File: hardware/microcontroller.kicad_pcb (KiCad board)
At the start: 2 copper layers, 50.8 x 78.7 mm, 45 parts, among them J5 1x2 jumper right-angle, J6 Conn_02x03_Odd_Even, J7 1x2 jumper right-angle, U1 74LVC2G125, U10 74HC670, U11 74HC670, U13 74AHC74, U15 74LVC138A, U17 74LVC138A, U18 74LVC2G125, U3 74LV163, U4 74LV163, U5 74LV163, U6 74LV163, U7 74LV163, U8 74LV164, U9 74LV164

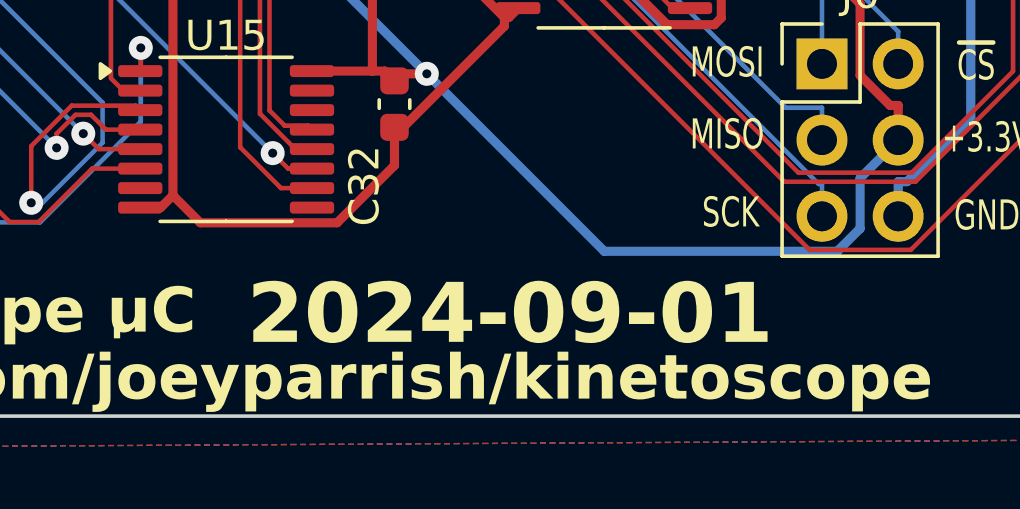
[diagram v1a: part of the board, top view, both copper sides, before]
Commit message: Improve uC board assembly process, fix minor bug
Changes to part numbers to better align with JLCPCB stock:
 - Replace 74LV164PW,118 / C179331 with SN74LV164APWR / C403720
 - Replace SN74LV163APWR / C2675453 with SN74LV161APWR / C2649404
   - Original had sync clear, but this is async clear, which is a bug
     fix!
 - Fix rotation of U8, U9, U13
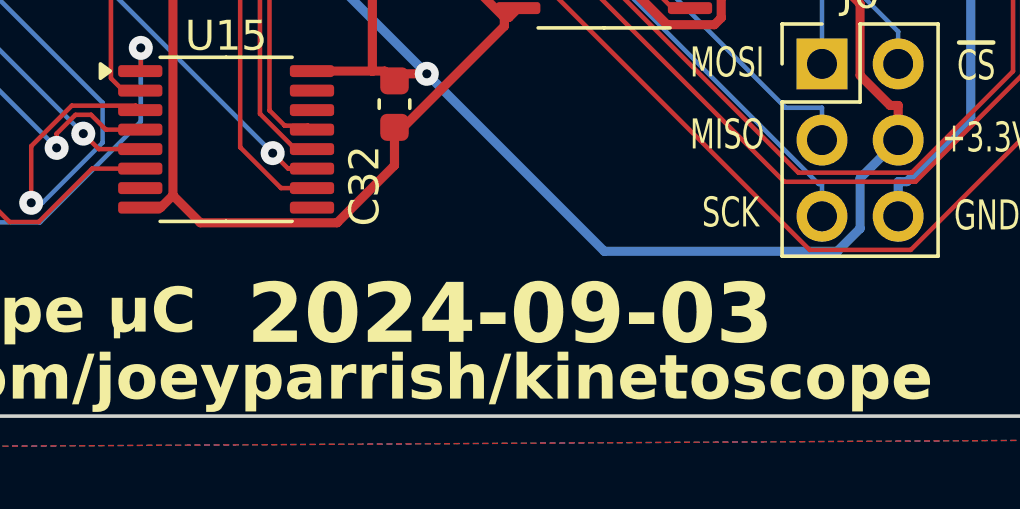
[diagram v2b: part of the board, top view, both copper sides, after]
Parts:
- U3, U4, U5, U6, U7: value 74LV163 -> 74LV161A
- U8, U9: value 74LV164 -> 74LV164A
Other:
- board text added: "2024-09-03"
- board text removed: "2024-09-01"
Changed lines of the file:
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@@
 			)
 		)
-		(property "Value" "74LV164"
+		(property "Value" "74LV164A"
 			(at 0 3.45 0)
 			(layer "F.Fab")
@@
 			)
 		)
-		(property "Datasheet" "https://www.mouser.com/datasheet/2/916/74LV164-1517637.pdf"
+		(property "Datasheet" "https://www.ti.com/lit/gpn/sn74lv164a"
 			(at 0 0 0)
 			(unlocked yes)
@@
 			)
 		)
-		(property "Mouser Part Number" "771-LV164PW118"
+		(property "Mouser Part Number" "595-SN74LV164APWR"
 			(at 0 0 0)
 			(unlocked yes)
@@
 			)
 		)
-		(property "Part Number" "74LV164PW,118"
+		(property "Part Number" "SN74LV164APWR"
 			(at 0 0 0)
 			(unlocked yes)
@@
 			)
 		)
-		(property "JLCPCB Part Number" "C179331"
+		(property "JLCPCB Part Number" "C403720"
 			(at 0 0 0)
 			(unlocked yes)
@@
 			)
 		)
-		(property "Value" "74LV164"
+		(property "Value" "74LV164A"
 			(at 0 3.45 0)
 			(layer "F.Fab")
@@
 			)
 		)
-		(property "Datasheet" "https://www.mouser.com/datasheet/2/916/74LV164-1517637.pdf"
+		(property "Datasheet" "https://www.ti.com/lit/gpn/sn74lv164a"
 			(at 0 0 0)
 			(unlocked yes)
@@
 			)
 		)
-		(property "Mouser Part Number" "771-LV164PW118"
+		(property "Mouser Part Number" "595-SN74LV164APWR"
 			(at 0 0 0)
 			(unlocked yes)
@@
 			)
 		)
-		(property "Part Number" "74LV164PW,118"
+		(property "Part Number" "SN74LV164APWR"
 			(at 0 0 0)
 			(unlocked yes)
@@
 			)
 		)
-		(property "JLCPCB Part Number" "C179331"
+		(property "JLCPCB Part Number" "C403720"
 			(at 0 0 0)
 			(unlocked yes)
@@
 			)
 		)
-		(property "Value" "74LV163"
+		(property "Value" "74LV161A"
 			(at 0 3.45 0)
 			(layer "F.Fab")
@@
 			)
 		)
-		(property "Datasheet" "https://www.ti.com/lit/gpn/sn74lv163a"
+		(property "Datasheet" "https://www.ti.com/lit/gpn/sn74lv161a"
 			(at 0 0 0)
 			(unlocked yes)
@@
 			)
 		)
-		(property "Mouser Part Number" "595-SN74LV163APWR"
+		(property "Mouser Part Number" "595-SN74LV161APWR"
 			(at 0 0 0)
 			(unlocked yes)
@@
 			)
 		)
-		(property "Part Number" "SN74LV163APWR"
+		(property "Part Number" "SN74LV161APWR"
 			(at 0 0 0)
 			(unlocked yes)
@@
 			)
 		)
-		(property "JLCPCB Part Number" "C2675453"
+		(property "JLCPCB Part Number" "C2649404"
 			(at 0 0 0)
 			(unlocked yes)
@@
 			)
 		)
-		(property "Value" "74LV163"
+		(property "Value" "74LV161A"
 			(at 0 3.45 0)
 			(layer "F.Fab")
@@
 			)
 		)
-		(property "Datasheet" "https://www.ti.com/lit/gpn/sn74lv163a"
+		(property "Datasheet" "https://www.ti.com/lit/gpn/sn74lv161a"
 			(at 0 0 0)
 			(unlocked yes)
@@
 			)
 		)
-		(property "Mouser Part Number" "595-SN74LV163APWR"
+		(property "Mouser Part Number" "595-SN74LV161APWR"
 			(at 0 0 0)
 			(unlocked yes)
@@
 			)
 		)
-		(property "Part Number" "SN74LV163APWR"
+		(property "Part Number" "SN74LV161APWR"
 			(at 0 0 0)
 			(unlocked yes)
@@
 			)
 		)
-		(property "JLCPCB Part Number" "C2675453"
+		(property "JLCPCB Part Number" "C2649404"
 			(at 0 0 0)
 			(unlocked yes)
@@
 			)
 		)
-		(property "Value" "74LV163"
+		(property "Value" "74LV161A"
 			(at 0 3.45 0)
 			(layer "F.Fab")
@@
 			)
 		)
-		(property "Datasheet" "https://www.ti.com/lit/gpn/sn74lv163a"
+		(property "Datasheet" "https://www.ti.com/lit/gpn/sn74lv161a"
 			(at 0 0 0)
 			(unlocked yes)
@@
 			)
 		)
-		(property "Mouser Part Number" "595-SN74LV163APWR"
+		(property "Mouser Part Number" "595-SN74LV161APWR"
 			(at 0 0 0)
 			(unlocked yes)
@@
 			)
 		)
-		(property "Part Number" "SN74LV163APWR"
+		(property "Part Number" "SN74LV161APWR"
 			(at 0 0 0)
 			(unlocked yes)
@@
 			)
 		)
-		(property "JLCPCB Part Number" "C2675453"
+		(property "JLCPCB Part Number" "C2649404"
 			(at 0 0 0)
 			(unlocked yes)
@@
 			)
 		)
-		(property "Value" "74LV163"
+		(property "Value" "74LV161A"
 			(at 0 3.45 0)
 			(layer "F.Fab")
@@
 			)
 		)
-		(property "Datasheet" "https://www.ti.com/lit/gpn/sn74lv163a"
+		(property "Datasheet" "https://www.ti.com/lit/gpn/sn74lv161a"
 			(at 0 0 0)
 			(unlocked yes)
@@
 			)
 		)
-		(property "Mouser Part Number" "595-SN74LV163APWR"
+		(property "Mouser Part Number" "595-SN74LV161APWR"
 			(at 0 0 0)
 			(unlocked yes)
@@
 			)
 		)
-		(property "Part Number" "SN74LV163APWR"
+		(property "Part Number" "SN74LV161APWR"
 			(at 0 0 0)
 			(unlocked yes)
@@
 			)
 		)
-		(property "JLCPCB Part Number" "C2675453"
+		(property "JLCPCB Part Number" "C2649404"
 			(at 0 0 0)
 			(unlocked yes)
@@
 			)
 		)
-		(property "Value" "74LV163"
+		(property "Value" "74LV161A"
 			(at 0 3.45 0)
 			(layer "F.Fab")
@@
 			)
 		)
-		(property "Datasheet" "https://www.ti.com/lit/gpn/sn74lv163a"
+		(property "Datasheet" "https://www.ti.com/lit/gpn/sn74lv161a"
 			(at 0 0 0)
 			(unlocked yes)
@@
 			)
 		)
-		(property "Mouser Part Number" "595-SN74LV163APWR"
+		(property "Mouser Part Number" "595-SN74LV161APWR"
 			(at 0 0 0)
 			(unlocked yes)
@@
 			)
 		)
-		(property "Part Number" "SN74LV163APWR"
+		(property "Part Number" "SN74LV161APWR"
 			(at 0 0 0)
 			(unlocked yes)
@@
 			)
 		)
-		(property "JLCPCB Part Number" "C2675453"
+		(property "JLCPCB Part Number" "C2649404"
 			(at 0 0 0)
 			(unlocked yes)
@@
 		)
 	)
-	(gr_text "2024-09-01"
+	(gr_text "2024-09-03"
 		(at 51.64 94.64 0)
 		(layer "F.SilkS")
@@
 			)
 		)
-		(render_cache "2024-09-01" 0
+		(render_cache "2024-09-03" 0
 			(polygon
 				(pts
@@
 			(polygon
 				(pts
-					(xy 59.076706 93.469162) (xy 59.332672 93.469162) (xy 59.332672 95.225757) (xy 59.839232 95.225757)
-					(xy 59.839232 95.47) (xy 58.556469 95.47) (xy 58.556469 95.225757) (xy 59.065471 95.225757) (xy 59.065471 93.843831)
-					(xy 58.727927 94.194075) (xy 58.590174 93.983538)
+					(xy 58.553538 93.469162) (xy 59.842163 93.469162) (xy 59.842163 93.738318) (xy 59.304829 94.282002)
+					(xy 59.538325 94.282002) (xy 59.842163 94.756322) (xy 59.842163 95.211591) (xy 59.594501 95.47)
+					(xy 58.553538 95.47) (xy 58.553538 95.225757) (xy 59.487522 95.225757) (xy 59.577892 95.136852)
+					(xy 59.577892 94.79247) (xy 59.39471 94.526245) (xy 58.980963 94.526245) (xy 58.980963 94.271256)
+					(xy 59.530021 93.713405) (xy 58.553538 93.713405)
 				)
 			)

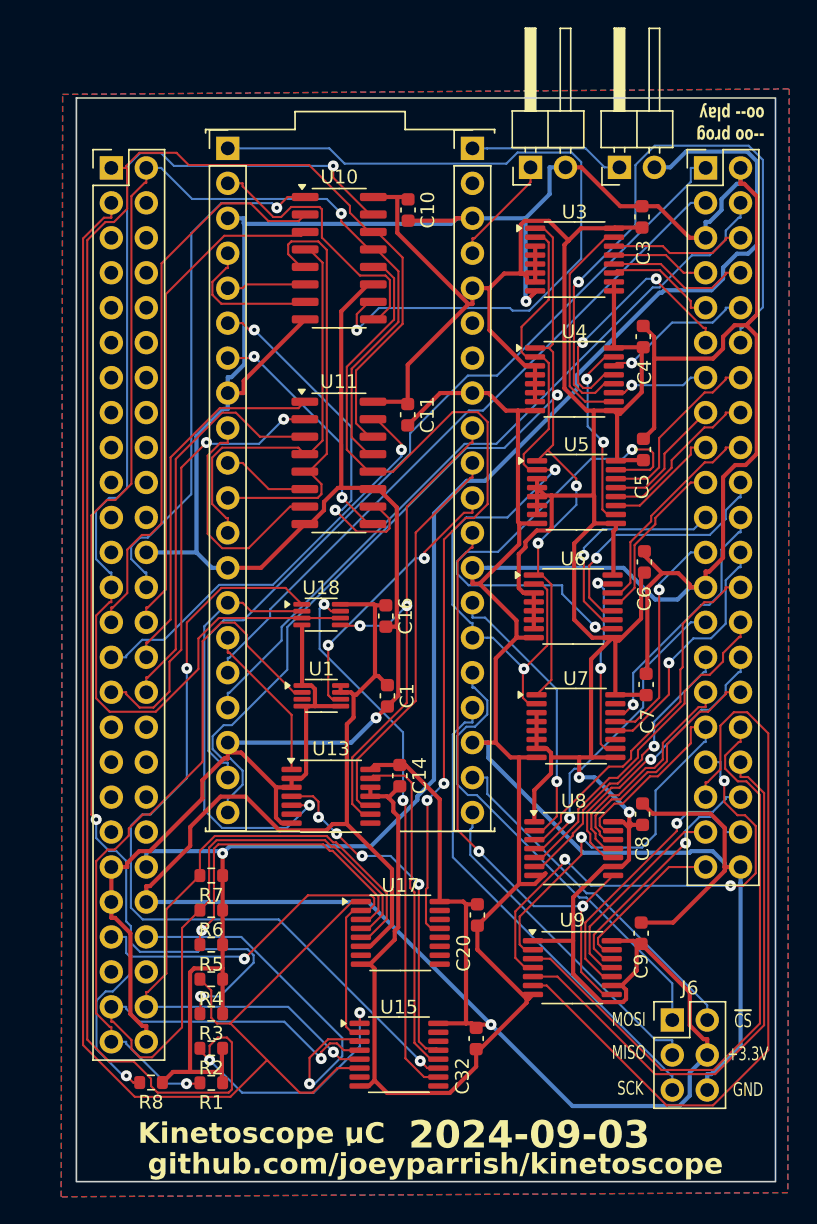
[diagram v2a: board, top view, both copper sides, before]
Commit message: Improve uC board assembly further
Change the register file CD74HC670M96 with SN74AHC373PWR and an
inverter, which is more easily available from JLCPCB.

This is not an exact replacement, as we replaced 2x 4x4 register files
with 2x 8-bit latches.  So instead of 4x 8-bit registers, we now only
have 2x 8-bit registers, but we only used 2 to begin with.

The new register hardware required us to change the address decoding
and the actual addresses of the registers.  Instead of 0xA13000 and
0xA13002, we now write to 0xA13010 and 0xA13012.
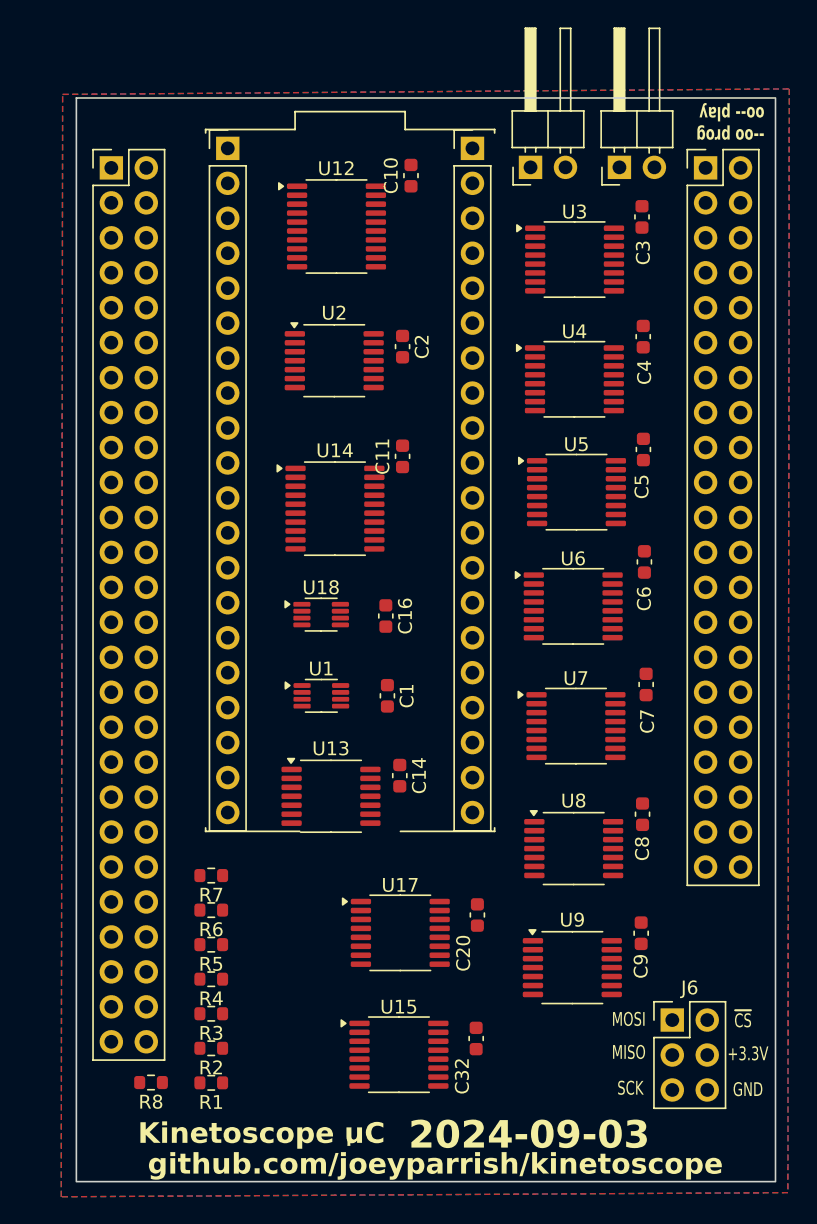
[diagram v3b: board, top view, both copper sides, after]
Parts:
- removed U10, U11: 74HC670, Package_SO:SOIC-16_3.9x9.9mm_P1.27mm
- added C2: 22nF, Capacitor_SMD:C_0603_1608Metric, F.Cu at (42.4, 37.4)
- added U12: 74AHC373, Package_SO:TSSOP-20_4.4x6.5mm_P0.65mm, F.Cu at (37.6, 28.6)
- added U14: 74AHC373, Package_SO:TSSOP-20_4.4x6.5mm_P0.65mm, F.Cu at (37.5, 49.1)
- added U2: 74AHC04, Package_SO:TSSOP-14_4.4x5mm_P0.65mm, F.Cu at (37.5, 38.4)
- moved C11 3.05 mm to (42.4, 45.3), turned to 90 degrees
- moved C10 2.51 mm to (43.1, 24.9), turned to 90 degrees
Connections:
- J3 pad 11: /REG_R_A0 -> /~{REG_0_OE}
- J3 pad 12: /REG_R_A1 -> /~{REG_1_OE}
- U17 pad 1: /kinetoscope-header-internal/SEGA_A3 -> /kinetoscope-header-internal/SEGA_A1
- U17 pad 12: unconnected-(U17-~{Y3}-Pad12) -> /~{REG_1_WE}
- U17 pad 13: /~{REG_WE} -> /~{REG_0_WE}
- U17 pad 6: +3.3V -> /kinetoscope-header-internal/SEGA_A4
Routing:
- net GND: track 468.2 -> 0.00 mm, vias 2 -> 0
- net +3.3V: track 351.6 -> 0.00 mm, vias 3 -> 0
- net /kinetoscope-header-internal/SEGA_A1: track 141.8 -> 0.00 mm, vias 2 -> 0
- net +5V: track 119.3 -> 0.00 mm, vias 1 -> 0
- net /kinetoscope-header-internal/SEGA_A2: track 113.3 -> 0.00 mm, vias 3 -> 0
- net /kinetoscope-header-internal/SEGA_A3: track 108.5 -> 0.00 mm
- net /~{SRAM_W_A_CLR}: track 85.4 -> 0.00 mm, vias 3 -> 0
- net /SEGA_D0: track 83.9 -> 0.00 mm, vias 1 -> 0
- net /~{REG_WE}: track 68.5 -> 0.00 mm, vias 2 -> 0
- net /~{SRAM_WE}: track 62.9 -> 0.00 mm
- net /~{SEGA_REGISTER}: track 61.0 -> 0.00 mm, vias 1 -> 0
- net /~{CMD_OE}: track 59.8 -> 0.00 mm, vias 2 -> 0
- net /SRAM_W_A_CLK: track 56.1 -> 0.00 mm, vias 2 -> 0
- net /SRAM_D_IN11: track 55.6 -> 0.00 mm
- net /REG_R_D0: track 55.1 -> 0.00 mm, vias 1 -> 0
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
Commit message: Add test pads to uC board
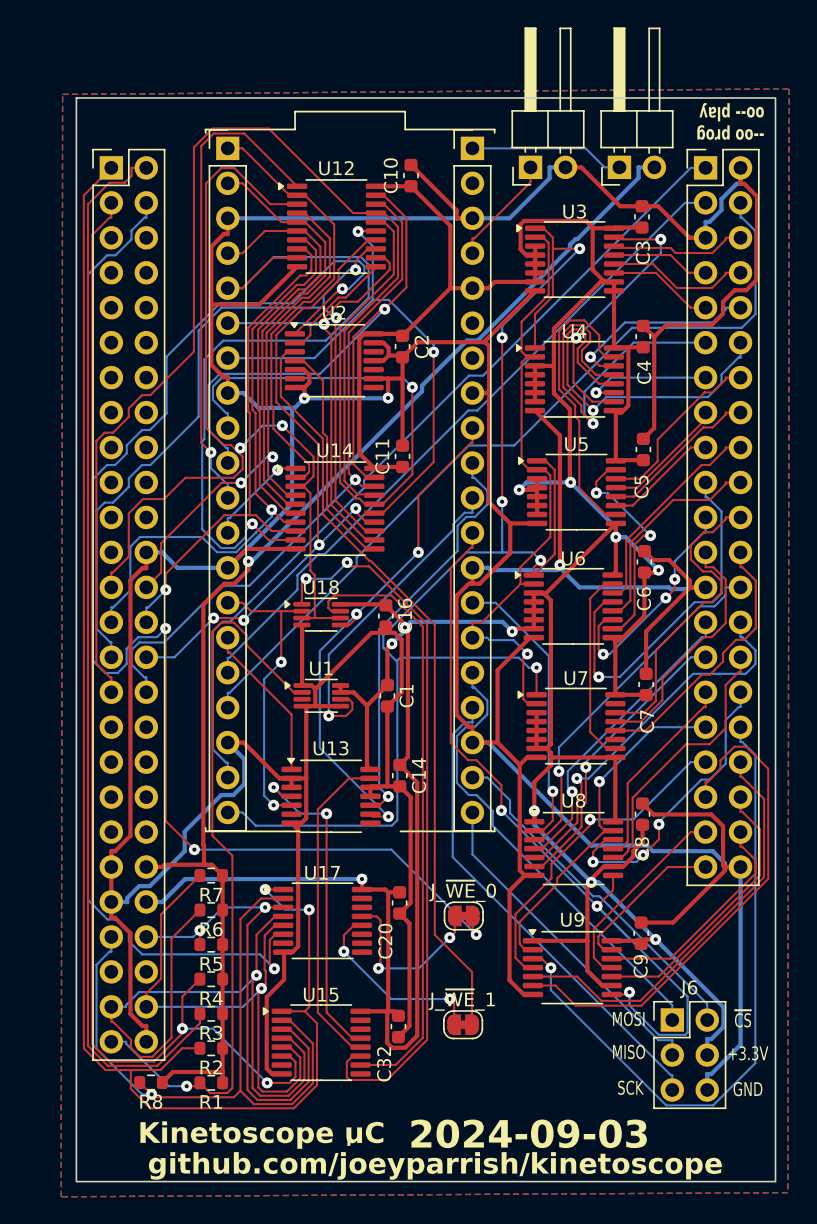
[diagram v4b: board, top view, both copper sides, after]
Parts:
- added J_~{WE}_0: ~, Jumper:SolderJumper-2_P1.3mm_Bridged_RoundedPad1.0x1.5mm, F.Cu at (46.9, 78.7)
- added J_~{WE}_1: ~, Jumper:SolderJumper-2_P1.3mm_Bridged_RoundedPad1.0x1.5mm, F.Cu at (46.8, 86.6)
- moved U17 5.72 mm to (36.6, 79.1)
- moved C20 5.72 mm to (42.2, 77.8)
- moved C32 5.72 mm to (42.1, 86.8)
- moved U15 5.72 mm to (36.5, 87.9)
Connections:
- U2 pad 1: /~{REG_0_WE} -> /~{REG_0_WE_INT}
- U2 pad 3: /~{REG_1_WE} -> /~{REG_1_WE_INT}
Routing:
- net GND: track 0.00 -> 485.7 mm, vias 0 -> 3
- net +3.3V: track 0.00 -> 315.9 mm, vias 0 -> 11
- net /kinetoscope-header-internal/SEGA_A1: track 0.00 -> 110.8 mm, vias 0 -> 2
- net /~{SRAM_W_A_CLR}: track 0.00 -> 101.0 mm, vias 0 -> 5
- net /~{REG_0_WE_INT}: track 0.00 -> 98.9 mm, vias 0 -> 4
- net +5V: track 0.00 -> 91.7 mm, vias 0 -> 1
- net /kinetoscope-header-internal/SEGA_A3: track 0.00 -> 86.5 mm, vias 0 -> 2
- net /SEGA_D6: track 0.00 -> 84.8 mm
- net /kinetoscope-header-internal/SEGA_A2: track 0.00 -> 77.5 mm
- net /kinetoscope-header-internal/SEGA_A4: track 0.00 -> 72.2 mm, vias 0 -> 1
- net /SEGA_D0: track 0.00 -> 68.9 mm, vias 0 -> 2
- net /SEGA_D4: track 0.00 -> 62.5 mm, vias 0 -> 2
- net /~{SRAM_WE}: track 0.00 -> 61.2 mm
- net /SRAM_DIS_2: track 0.00 -> 59.8 mm
- net /SRAM_D_CLK: track 0.00 -> 58.1 mm, vias 0 -> 3
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
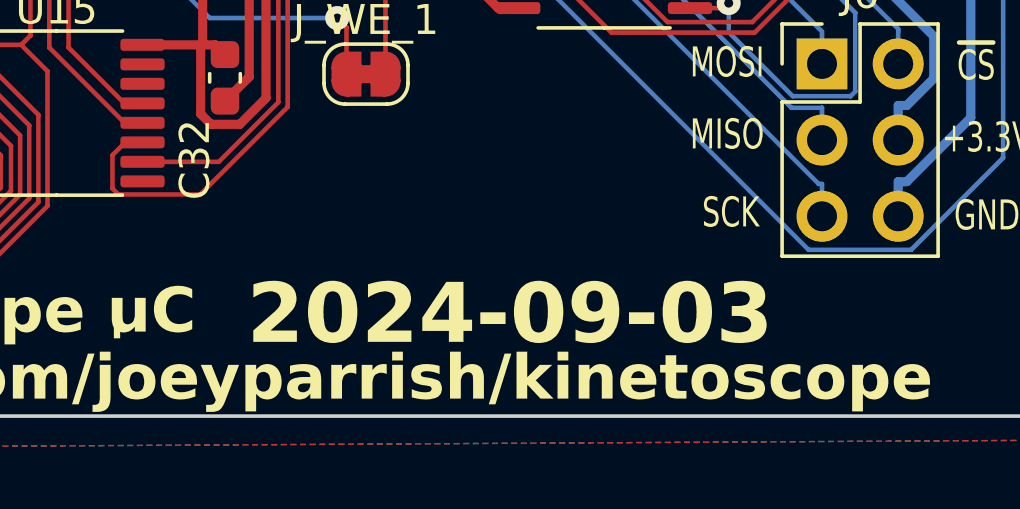
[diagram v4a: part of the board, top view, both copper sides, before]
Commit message: Fix footprint for new SMD regulator
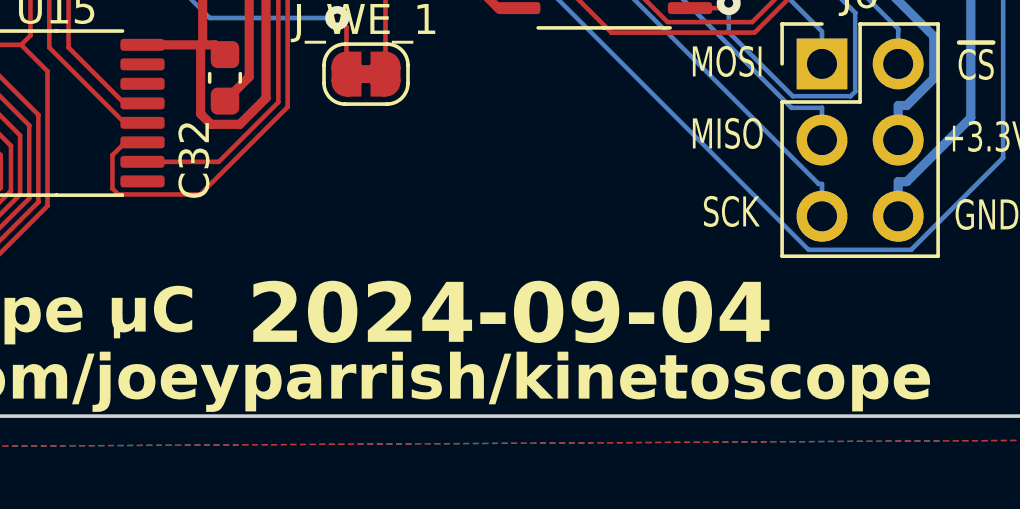
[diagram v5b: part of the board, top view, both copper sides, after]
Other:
- board text added: "2024-09-04"
- board text removed: "2024-09-03"
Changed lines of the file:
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@@
 		)
 	)
-	(gr_text "2024-09-03"
+	(gr_text "2024-09-04"
 		(at 51.64 94.64 0)
 		(layer "F.SilkS")
@@
 			)
 		)
-		(render_cache "2024-09-03" 0
+		(render_cache "2024-09-04" 0
 			(polygon
 				(pts
@@
 			(polygon
 				(pts
-					(xy 58.553538 93.469162) (xy 59.842163 93.469162) (xy 59.842163 93.738318) (xy 59.304829 94.282002)
-					(xy 59.538325 94.282002) (xy 59.842163 94.756322) (xy 59.842163 95.211591) (xy 59.594501 95.47)
-					(xy 58.553538 95.47) (xy 58.553538 95.225757) (xy 59.487522 95.225757) (xy 59.577892 95.136852)
-					(xy 59.577892 94.79247) (xy 59.39471 94.526245) (xy 58.980963 94.526245) (xy 58.980963 94.271256)
-					(xy 59.530021 93.713405) (xy 58.553538 93.713405)
+					(xy 59.757655 94.56337) (xy 59.926671 94.56337) (xy 59.926671 94.807613) (xy 59.757655 94.807613)
+					(xy 59.757655 95.47) (xy 59.490453 95.47) (xy 59.490453 94.807613) (xy 58.742093 94.807613) (xy 58.489984 94.437341)
+					(xy 58.775799 94.437341) (xy 58.863238 94.56337) (xy 59.490453 94.56337) (xy 59.490453 93.703147)
+					(xy 58.775799 94.437341) (xy 58.489984 94.437341) (xy 58.46903 94.406566) (xy 59.369309 93.469162)
+					(xy 59.757655 93.469162)
 				)
 			)
